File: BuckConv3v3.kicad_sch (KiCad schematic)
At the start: 9 parts, among them U4 TPS5430DDA

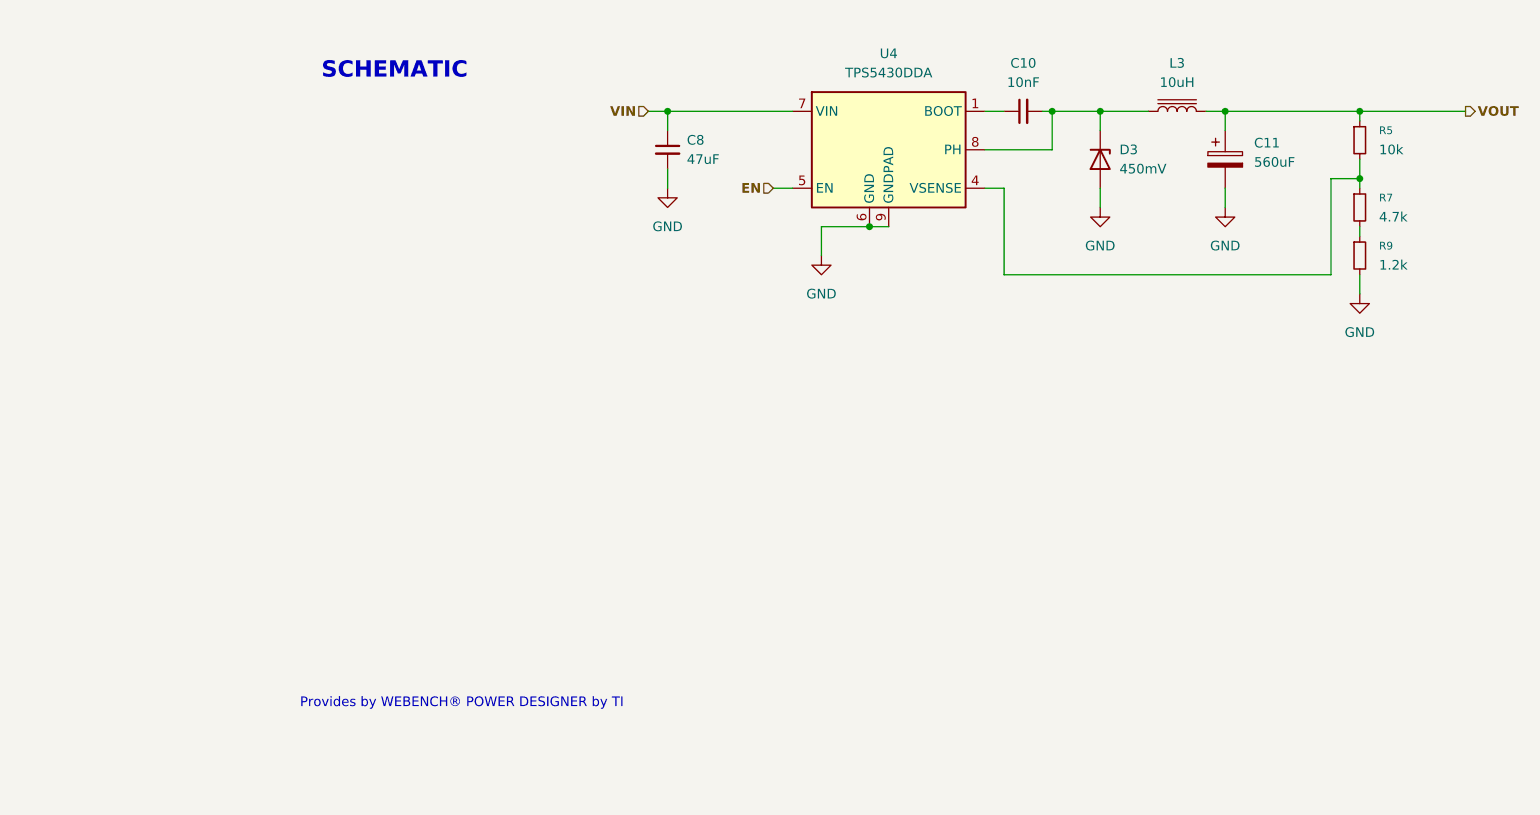
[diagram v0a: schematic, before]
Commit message: Semi finished the regulator-section
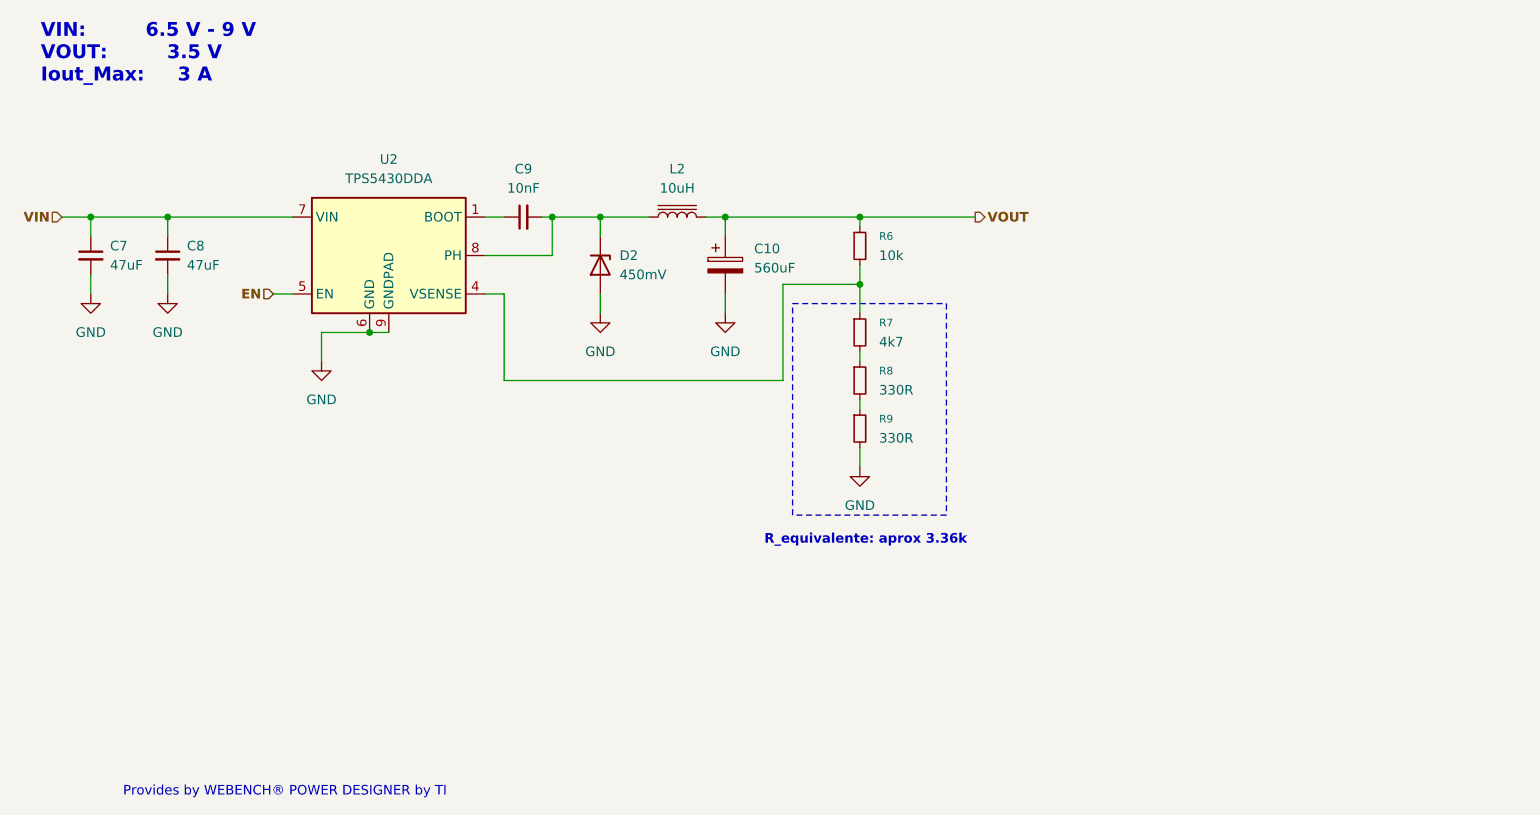
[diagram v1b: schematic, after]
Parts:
- added C7: 47uF, Capacitor_SMD:C_0805_2012Metric, symbol Device:C_Small
- added R8: 330R, Resistor_SMD:R_0805_2012Metric, symbol Device:R_Small
- C10: renamed from C11; footprint (none) -> Capacitor_SMD:C_0805_2012Metric
- C8: footprint (none) -> Capacitor_SMD:C_0805_2012Metric
- C9: renamed from C10; footprint (none) -> Capacitor_SMD:C_0805_2012Metric
- D2: renamed from D3; footprint (none) -> Capacitor_SMD:C_0805_2012Metric
- L2: renamed from L3; footprint (none) -> Inductor_SMD:L_Sumida_CDMC6D28_7.25x6.5mm
- R6: renamed from R5; footprint (none) -> Resistor_SMD:R_0805_2012Metric
- R7: value 4.7k -> 4k7; footprint (none) -> Resistor_SMD:R_0805_2012Metric
- R9: value 1.2k -> 330R; footprint (none) -> Resistor_SMD:R_0805_2012Metric
- renumbered U4 to U2
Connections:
- net GND: now also C7.2
- net VIN: now also C7.1
- net at R9.1: now also R8.2; no longer R7.2
- new net: R7.2, R8.1
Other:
- note added: "R_equivalente: aprox 3.36k"
- note added: "VIN: 6.5 V - 9 V VOUT: 3.5 V Iout_Max: 3 A"
- note removed: "SCHEMATIC"
- moved on the sheet: C10, C8, C9, D2, L2, R6, R7, R9, U2
